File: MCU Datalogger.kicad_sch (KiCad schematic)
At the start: 11 parts

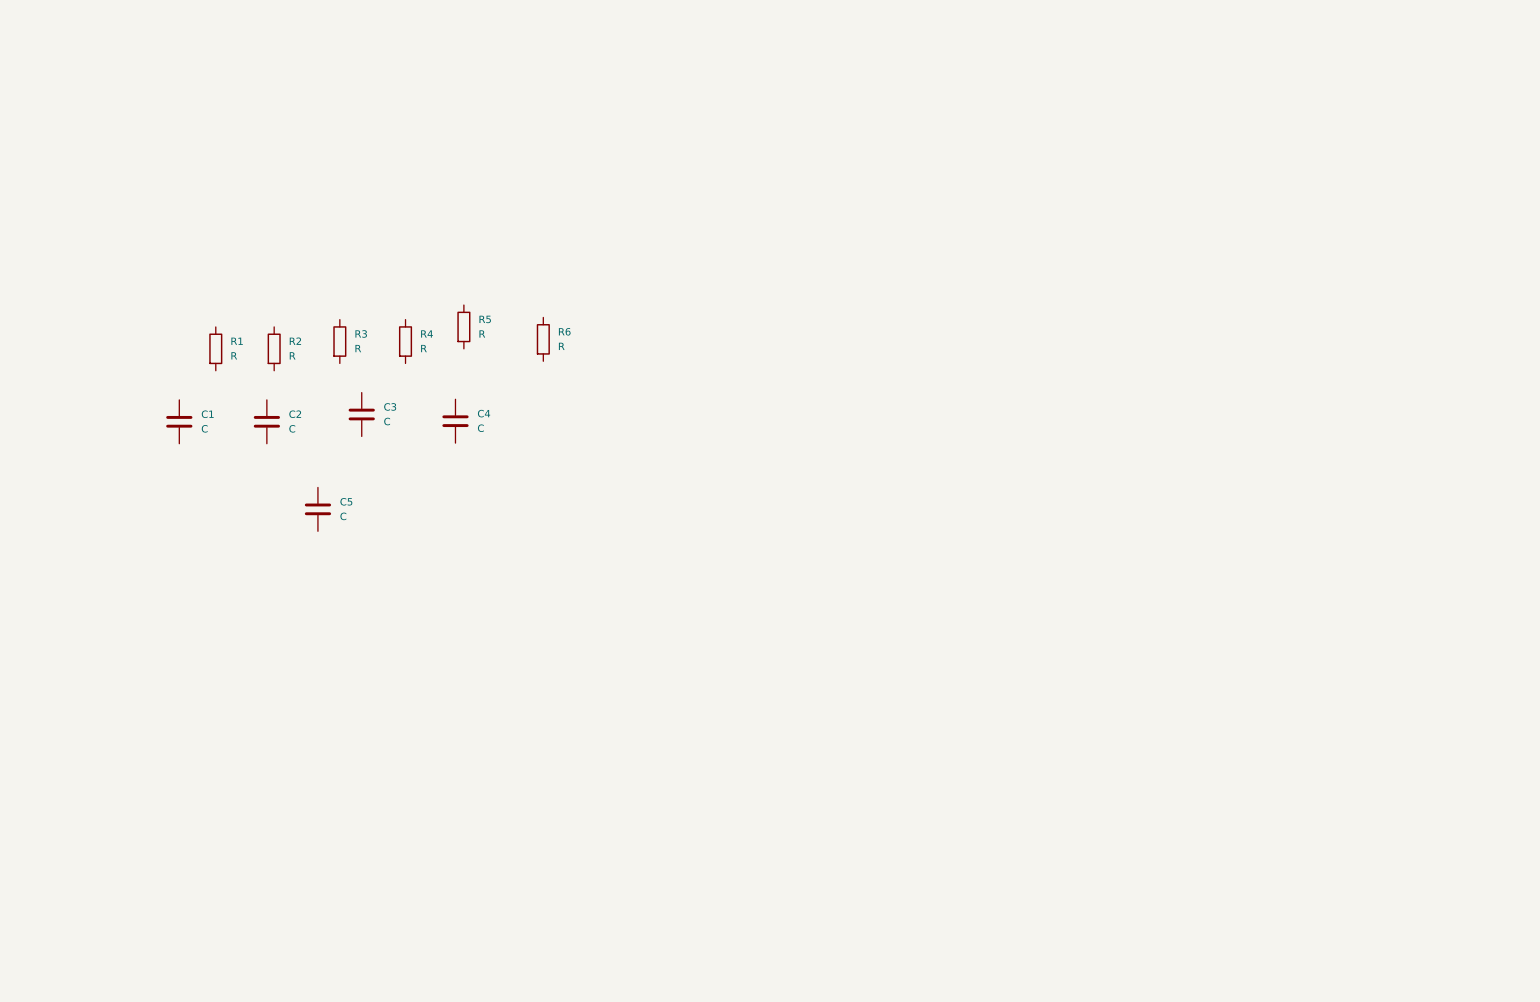
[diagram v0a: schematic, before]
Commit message: all symbols were added to the schematic
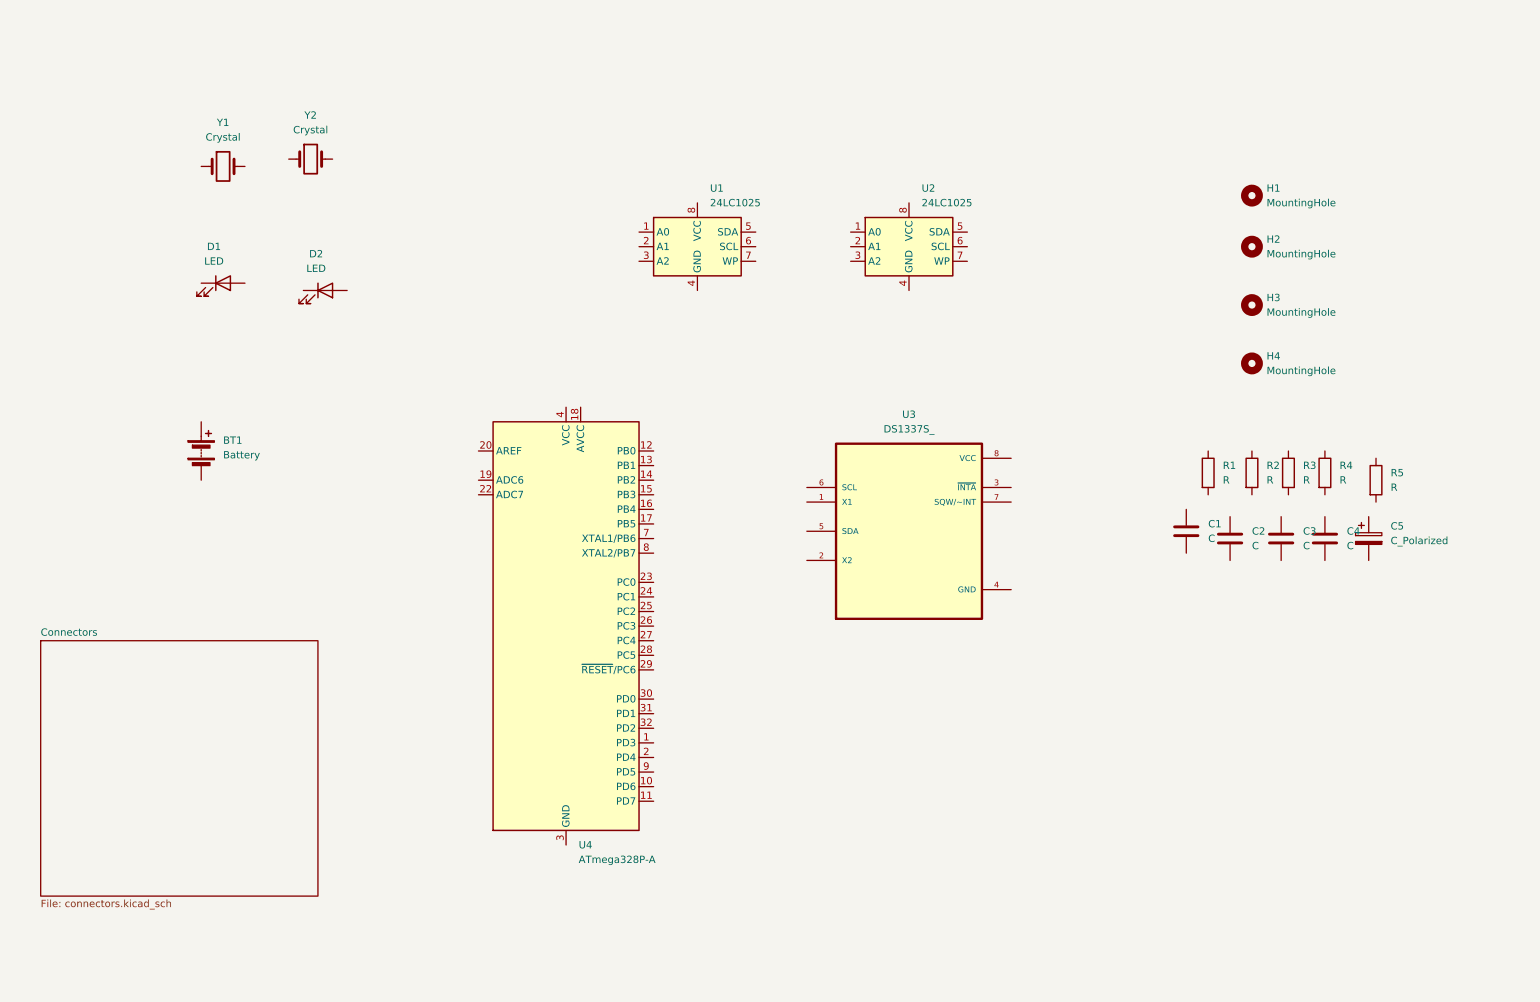
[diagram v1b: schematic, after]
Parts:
- removed C5: C, symbol Device:C
- removed R6: R, symbol Device:R
- added BT1: Battery, symbol Device:Battery
- added C5: C_Polarized, symbol Device:C_Polarized
- added D1, D2: LED, symbol Device:LED
- added H1, H2, H3, H4: MountingHole, symbol Mechanical:MountingHole
- added U1, U2: 24LC1025, symbol Memory_EEPROM:24LC1025
- added U3: DS1337S_, DS1337S_:SOIC127P600X175-8N, symbol DS1337S_:DS1337S_
- added U4: ATmega328P-A, Package_QFP:TQFP-32_7x7mm_P0.8mm, symbol MCU_Microchip_ATmega:ATmega328P-A
- added Y1, Y2: Crystal, symbol Device:Crystal
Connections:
- new net: U4.21 (GND), U4.3 (GND), U4.5 (GND)
- new net: U4.4 (VCC), U4.6 (VCC)
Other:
- added sheet Connectors (connectors.kicad_sch)
- company: (none) -> Lucas Vinicius 
- title: (none) -> ${project_name}

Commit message: updating the project with all necessary component libraries
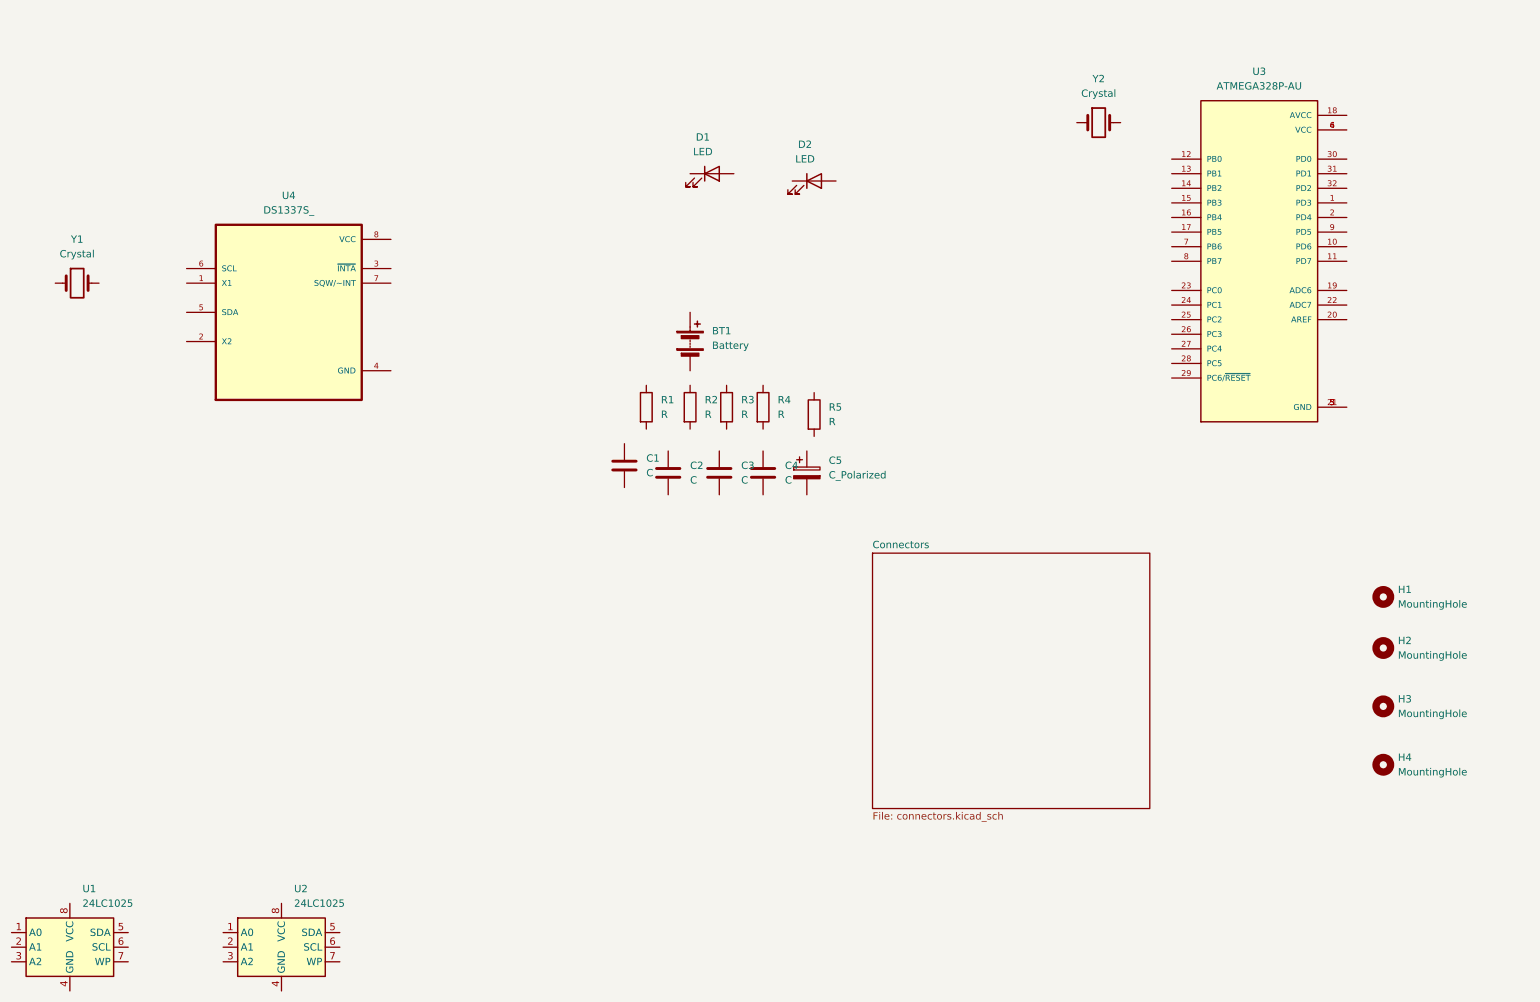
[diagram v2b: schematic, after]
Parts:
- removed U3: DS1337S_, DS1337S_:SOIC127P600X175-8N, symbol DS1337S_:DS1337S_
- removed U4: ATmega328P-A, Package_QFP:TQFP-32_7x7mm_P0.8mm, symbol MCU_Microchip_ATmega:ATmega328P-A
- added U3: ATMEGA328P-AU, ATMEGA328P-AU:QFP80P900X900X120-32N, symbol ATMEGA328P-AU:ATMEGA328P-AU
- added U4: DS1337S_, DS1337S_:SOIC127P600X175-8N, symbol DS1337S_:DS1337S_
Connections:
- new net: U3.21 (GND), U3.3 (GND), U3.5 (GND)
- new net: U3.4 (VCC), U3.6 (VCC)
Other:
- moved on the sheet: BT1, C1, C2, C3, C4, C5, D1, D2, H1, H2, H3, H4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

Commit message: added values to the components
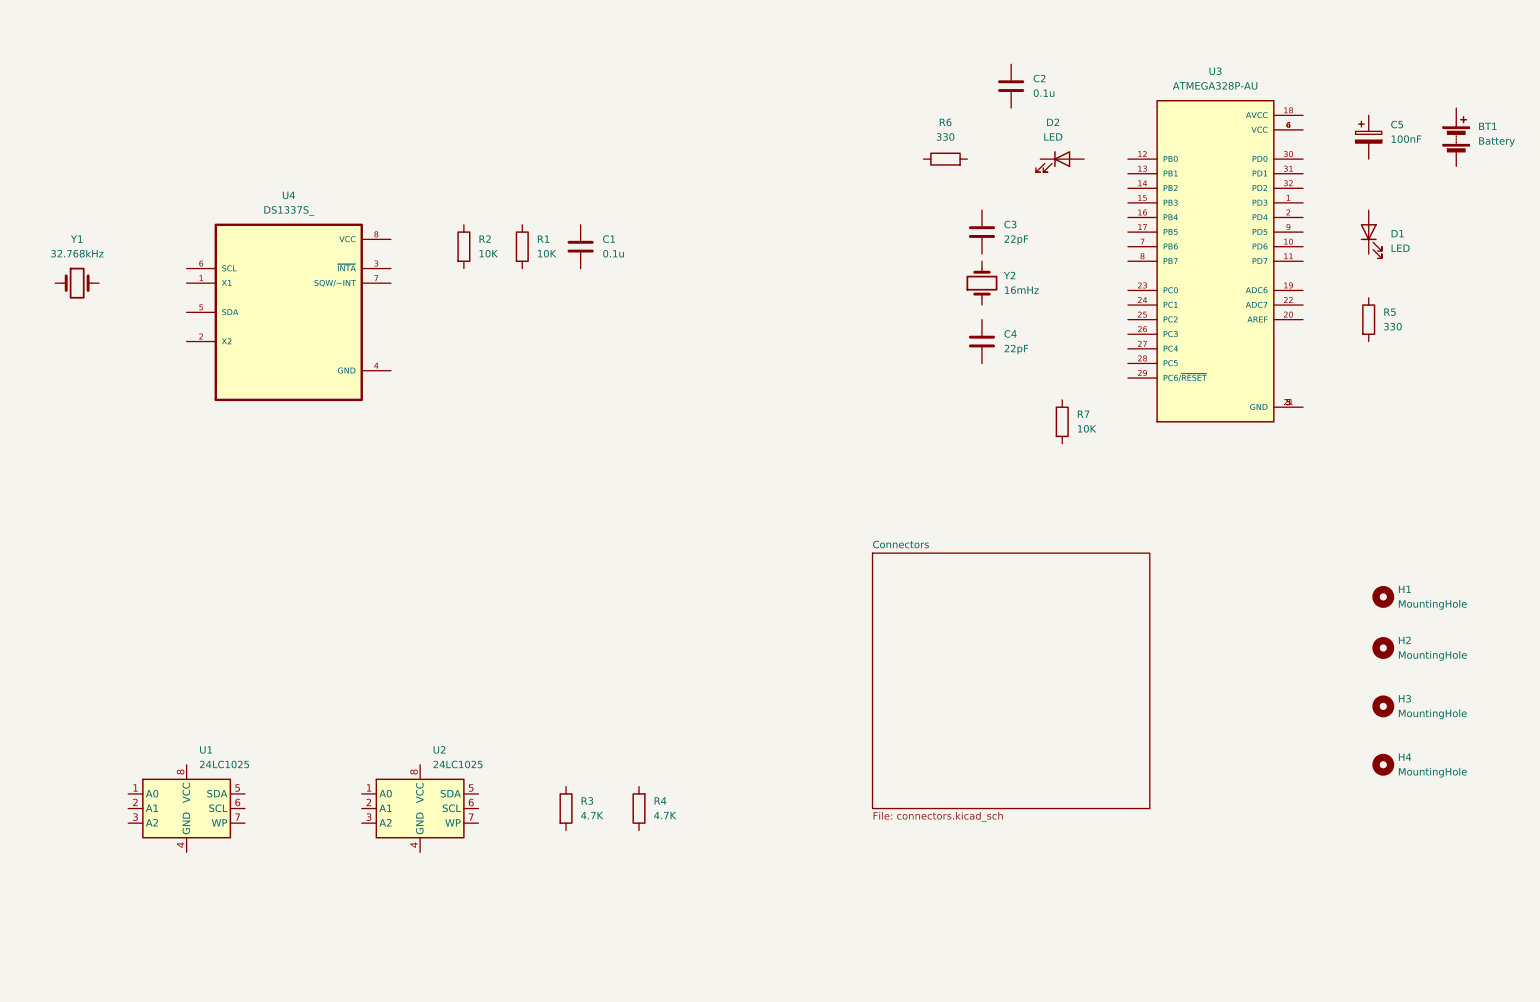
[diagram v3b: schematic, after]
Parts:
- added R6: 330, symbol Device:R
- added R7: 10K, symbol Device:R
- C1, C2: value C -> 0.1u
- C3, C4: value C -> 22pF
- C5: value C_Polarized -> 100nF
- R1, R2: value R -> 10K
- R3, R4: value R -> 4.7K
- R5: value R -> 330
- Y1: value Crystal -> 32.768kHz
- Y2: value Crystal -> 16mHz
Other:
- moved on the sheet: BT1, C1, C2, C3, C4, C5, D1, D2, R1, R2, R3, R4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

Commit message: proceeded to wire all the components on the first sheet
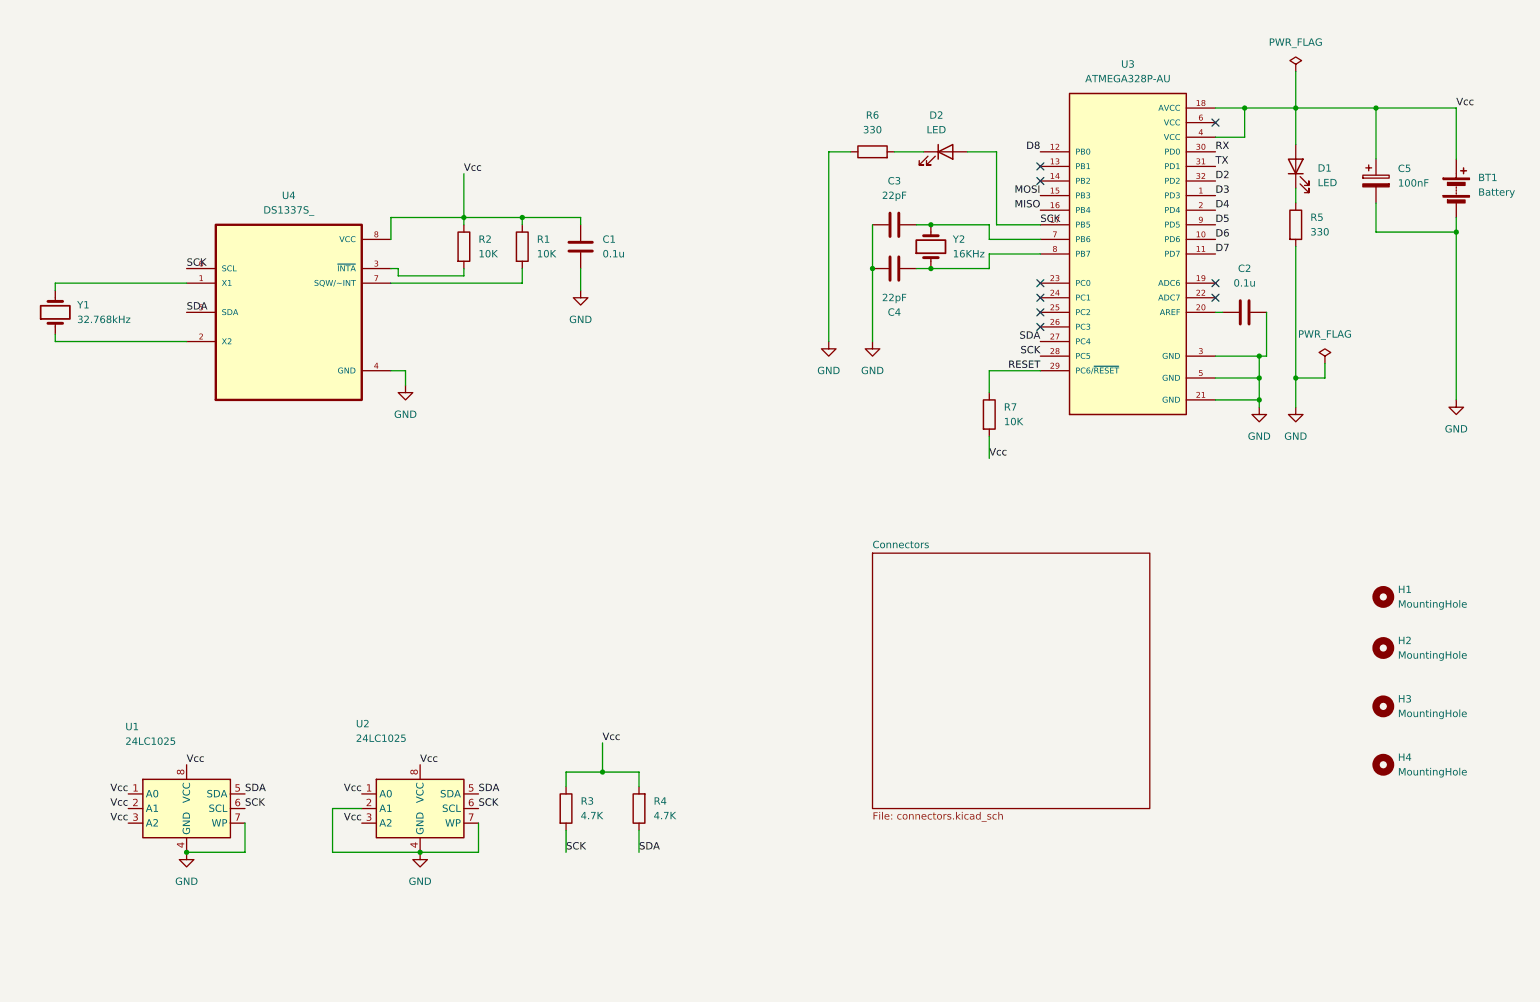
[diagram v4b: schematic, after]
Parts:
- BT1: footprint (none) -> Connector_PinHeader_2.54mm:PinHeader_1x02_P2.54mm_Vertical
- C1, C2, C3, C4, C5: footprint (none) -> Capacitor_SMD:C_0805_2012Metric_Pad1.18x1.45mm_HandSolder
- D1, D2: footprint (none) -> LED_SMD:LED_0805_2012Metric_Pad1.15x1.40mm_HandSolder
- H1, H2, H3, H4: footprint (none) -> MountingHole:MountingHole_2.1mm
- R1, R2, R3, R4, R5, R6, R7: footprint (none) -> Resistor_SMD:R_0805_2012Metric_Pad1.20x1.40mm_HandSolder
- U1, U2: footprint (none) -> Package_SO:SOIC-8_5.23x5.23mm_P1.27mm
- Y1: footprint (none) -> Crystal:Crystal_SMD_5032-2Pin_5.0x3.2mm_HandSoldering
- Y2: value 16mHz -> 16KHz; footprint (none) -> Crystal:Crystal_SMD_5032-2Pin_5.0x3.2mm_HandSoldering
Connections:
- net at D2.1 (K): now also R6.2
- net SCK: now reaches D2.2 (A)
- net SCK: now also R3.2, U1.6 (SCL), U2.6 (SCL), U3.17 (PB5), U3.28 (PC5), U4.6 (SCL)
- net at R5.1: now also D1.1 (K)
- net GND: now reaches R5.2
- net GND: now also BT1.2 (-), C1.2, C2.2, C3.1, C4.2, C5.2, R6.1, U1.4 (GND), U1.7 (WP), U2.2 (A1), U2.4 (GND), U2.7 (WP), U3.21 (GND), U3.3 (GND), U3.5 (GND), U4.4 (GND)
- net Vcc: now reaches R1.1
- net Vcc: now also BT1.1 (+), C1.1, C5.1, D1.2 (A), R2.1, R3.1, R4.2, R7.2, U1.1 (A0), U1.2 (A1), U1.3 (A2), U1.8 (VCC), U2.1 (A0), U2.3 (A2), U2.8 (VCC), U3.18 (AVCC), U3.4 (VCC), U4.8 (VCC)
- net at R1.2: now also U4.7 (SQW/~INT)
- net at C2.1: now also U3.20 (AREF)
- net D3: now reaches U3.1 (PD3)
- net D6: now reaches U3.10 (PD6)
- net D7: now reaches U3.11 (PD7)
- net D8: now reaches U3.12 (PB0)
- net MOSI: now reaches U3.15 (PB3)
- net MISO: now reaches U3.16 (PB4)
- net D4: now reaches U3.2 (PD4)
- net SDA: now reaches U3.27 (PC4)
- net SDA: now also R4.1, U1.5 (SDA), U2.5 (SDA), U4.5 (SDA)
- net RESET: now reaches U3.29 (PC6/~{RESET})
- net RESET: now also R7.1
- net RX: now reaches U3.30 (PD0)
- net TX: now reaches U3.31 (PD1)
- net D2: now reaches U3.32 (PD2)
- net at U3.6 (VCC): no longer U3.4 (VCC)
- net at U3.7 (PB6): now also C3.2, Y2.2
- net at U3.8 (PB7): now also C4.1, Y2.1
- net D5: now reaches U3.9 (PD5)
- net at U4.1 (X1): now also Y1.2
- net at U4.2 (X2): now also Y1.1
- net at U4.3 (~{INTA}): now also R2.2
- no-connect marks 0 -> 9
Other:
- moved on the sheet: BT1, C2, C3, C4, C5, D1, D2, R5, R6, R7, Y1, Y2

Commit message: the sheet is fully wired ready for an ERC
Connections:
- net Vcc: no longer BT1.1 (+), C5.1, D1.2 (A), U3.18 (AVCC), U3.4 (VCC)
- new net: BT1.1 (+), C5.1, D1.2 (A), U3.18 (AVCC), U3.4 (VCC)
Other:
- sheet Connectors ports: added D2, D3, D4, D5, D6, D7, D8, GND, MISO, MOSI, RESET, RX, SCK, SDA, TX, Vcc; removed none

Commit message: the net classes were set up and the schematic was properly labeled
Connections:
- net Vcc: now also BT1.1 (+), C5.1, D1.2 (A), U3.18 (AVCC), U3.4 (VCC)
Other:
- note added: "EEPROM"
- note added: "MCU"
- note added: "Mounting"
- note added: "Real Time Clock"
